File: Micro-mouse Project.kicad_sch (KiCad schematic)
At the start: 29 parts, among them IC1 CH224K, J1 Conn_02x16_Odd_Even, J3 USB_C_Receptacle_USB2.0_16P, Q2 2N3904, U2 LM2596S-5, U4 INA219AxD, U7 TP4056-42-ESOP8

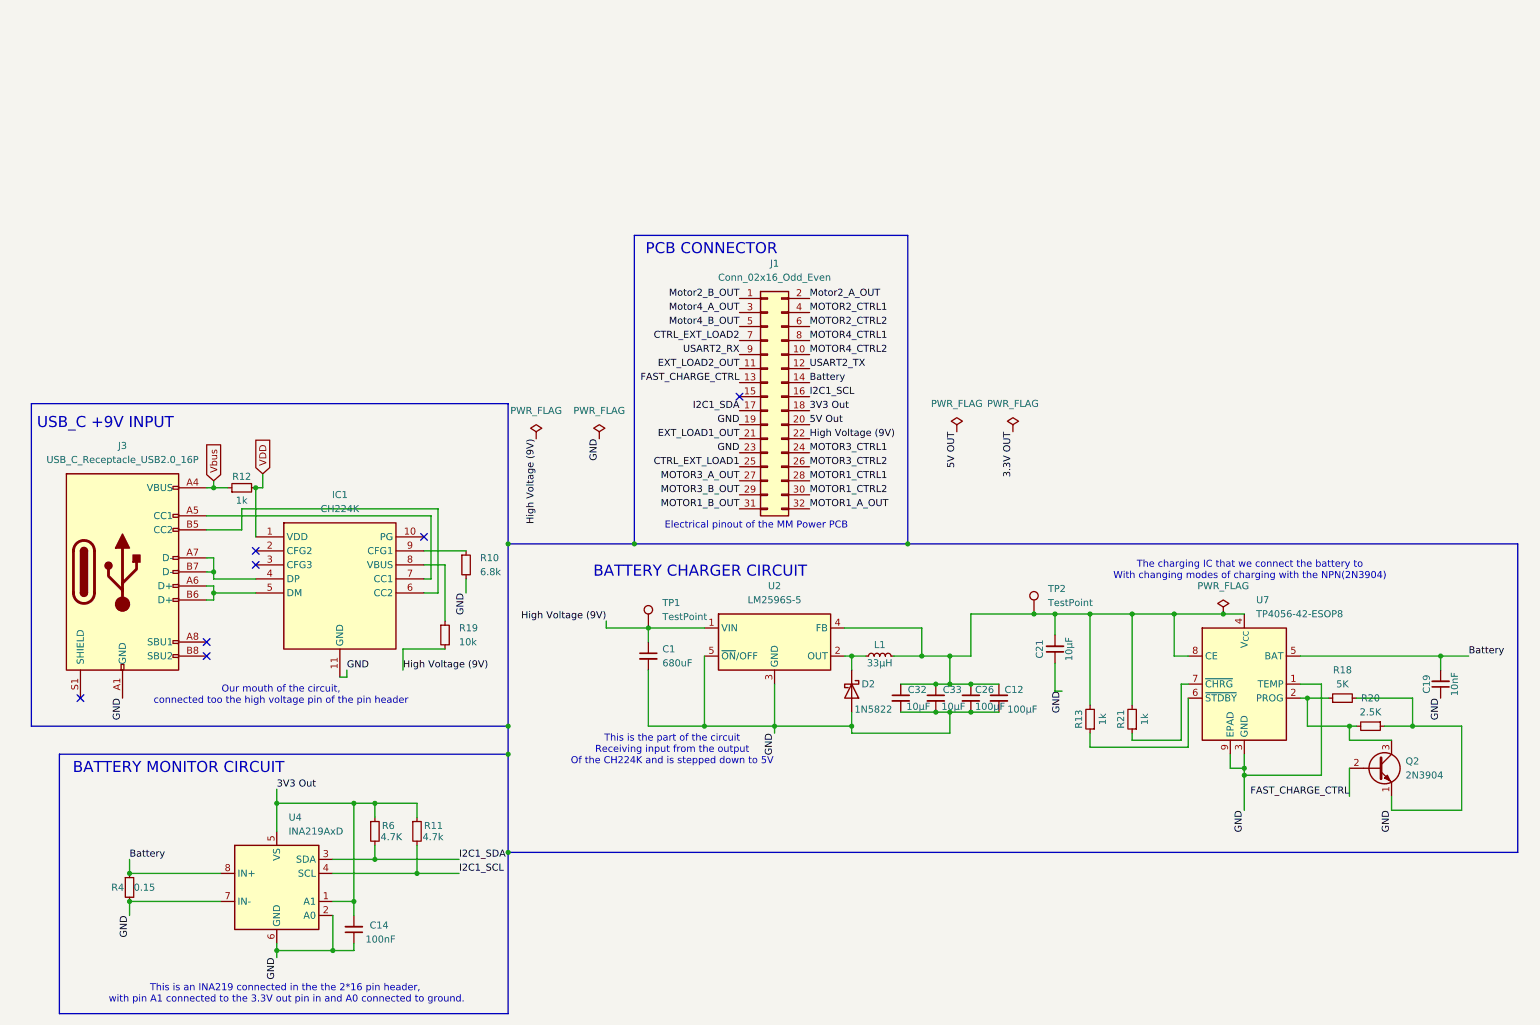
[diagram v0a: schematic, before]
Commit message: The Motor Management Circuit
This caters for the motor and the switching ON/OFF of the power subsystem.
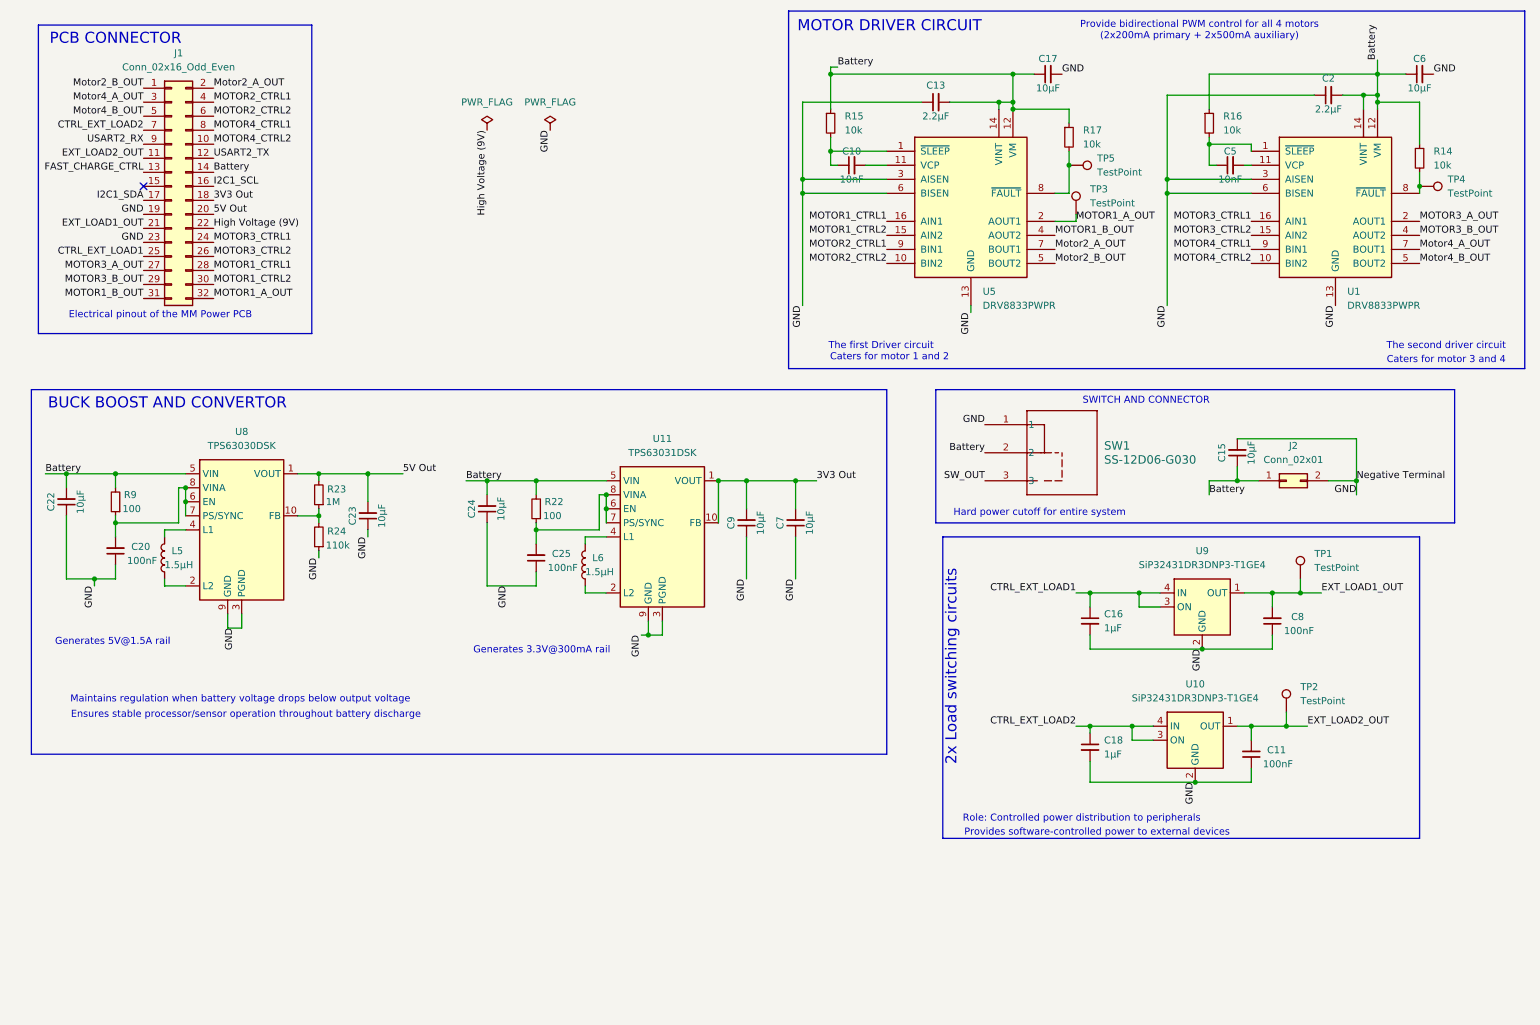
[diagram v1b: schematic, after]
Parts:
- removed C1: 680uF, Capacitor_THT:CP_Axial_L18.0mm_D10.0mm_P25.00mm_Horizontal, symbol Device:C_Small
- removed C12, C26: 100μF, Capacitor_SMD:C_1206_3216Metric_Pad1.33x1.80mm_HandSolder, symbol Device:C_Small
- removed C14: 100nF, Capacitor_SMD:C_0402_1005Metric_Pad0.74x0.62mm_HandSolder, symbol Device:C_Small
- removed C19: 10nF, Capacitor_SMD:C_0805_2012Metric_Pad1.18x1.45mm_HandSolder, symbol Device:C_Small
- removed C21: 10μF, Capacitor_SMD:C_1206_3216Metric_Pad1.33x1.80mm_HandSolder, symbol Device:C_Small
- removed C32, C33: 10μF, Capacitor_SMD:C_0805_2012Metric_Pad1.18x1.45mm_HandSolder, symbol Device:C_Small
- removed D2: 1N5822, Library:DIO_SS34, symbol Diode:1N5822
- removed IC1: CH224K, Library:SOP100P600X180-11N, symbol CH224K:CH224K
- removed J3: USB_C_Receptacle_USB2.0_16P, Connector_USB:USB_C_Receptacle_GCT_USB4105-xx-A_16P_TopMnt_Horizontal, symbol Connector:USB_C_Receptacle_USB2.0_16P
- removed L1: 33μH, Inductor_THT:L_Axial_L20.0mm_D8.0mm_P25.40mm_Horizontal, symbol Device:L_Small
- removed Q2: 2N3904, Package_TO_SOT_SMD:SOT-23, symbol Transistor_BJT:2N3904
- removed R10: 6.8k, Resistor_SMD:R_0603_1608Metric_Pad0.98x0.95mm_HandSolder, symbol Device:R_Small
- removed R11: 4.7k, Resistor_SMD:R_0603_1608Metric_Pad0.98x0.95mm_HandSolder, symbol Device:R_Small
- removed R12, R13, R21: 1k, Resistor_SMD:R_1206_3216Metric_Pad1.30x1.75mm_HandSolder, symbol Device:R_Small
- removed R18: 5K, Resistor_SMD:R_0603_1608Metric, symbol Device:R_Small
- removed R19: 10k, Resistor_SMD:R_0805_2012Metric_Pad1.20x1.40mm_HandSolder, symbol Device:R_Small
- removed R20: 2.5K, Resistor_SMD:R_0603_1608Metric, symbol Device:R_Small
- removed R4: 0.15, Resistor_SMD:R_1206_3216Metric_Pad1.30x1.75mm_HandSolder, symbol Device:R_Small
- removed R6: 4.7K, Resistor_SMD:R_0603_1608Metric_Pad0.98x0.95mm_HandSolder, symbol Device:R_Small
- removed U2: LM2596S-5, Package_TO_SOT_SMD:TO-263-5_TabPin3, symbol Regulator_Switching:LM2596S-5
- removed U4: INA219AxD, Library:SOT65P280X145-8N, symbol Sensor_Energy:INA219AxD
- removed U7: TP4056-42-ESOP8, Library:SOIC127P600X175-9N, symbol Battery_Management:TP4056-42-ESOP8
- added C10, C5: 10nF, Capacitor_SMD:C_0805_2012Metric_Pad1.18x1.45mm_HandSolder, symbol Device:C_Small
- added C11, C20, C25, C8: 100nF, Capacitor_SMD:C_0402_1005Metric_Pad0.74x0.62mm_HandSolder, symbol Device:C_Small
- added C13, C2: 2.2μF, Capacitor_SMD:C_0402_1005Metric_Pad0.74x0.62mm_HandSolder, symbol Device:C_Small
- added C15, C17, C22, C23, C24, C6, C7, C9: 10μF, Capacitor_SMD:C_1206_3216Metric_Pad1.33x1.80mm_HandSolder, symbol Device:C_Small
- added C16, C18: 1μF, Capacitor_SMD:C_1206_3216Metric_Pad1.33x1.80mm_HandSolder, symbol Device:C_Small
- added J2: Conn_02x01, symbol Connector_Generic:Conn_02x01
- added L5, L6: 1.5µH, Inductor_SMD:L_1206_3216Metric_Pad1.22x1.90mm_HandSolder, symbol Device:L
- added R14, R15, R16, R17: 10k, Resistor_SMD:R_0805_2012Metric_Pad1.20x1.40mm_HandSolder, symbol Device:R_Small
- added R22, R9: 100, Resistor_SMD:R_0805_2012Metric_Pad1.20x1.40mm_HandSolder, symbol Device:R_Small
- added R23: 1M, Resistor_SMD:R_1206_3216Metric_Pad1.30x1.75mm_HandSolder, symbol Device:R_Small
- added R24: 110k, Resistor_SMD:R_0805_2012Metric_Pad1.20x1.40mm_HandSolder, symbol Device:R_Small
- added SW1: SS-12D06-G030, Library:SS-12D06_GSW, symbol 2025-03-28_06-57-30:SS-12D06-G030
- added TP3, TP4, TP5: TestPoint, symbol Connector:TestPoint
- added U1, U5: DRV8833PWPR, Library:IC_DRV8833PWPR, symbol Driver_Motor:DRV8833PWP
- added U10: SiP32431DR3DNP3-T1GE4, Library:SON50P120X160X60-5N, symbol Power_Management:SiP32431DR3
- added U11: TPS63031DSK, Package_SON:WSON-10-1EP_2.5x2.5mm_P0.5mm_EP1.2x2mm, symbol Regulator_Switching:TPS63031DSK
- added U8: TPS63030DSK, Package_SON:WSON-10-1EP_2.5x2.5mm_P0.5mm_EP1.2x2mm, symbol Regulator_Switching:TPS63030DSK
- added U9: SiP32431DR3DNP3-T1GE4, Package_TO_SOT_SMD:SOT-363_SC-70-6, symbol Power_Management:SiP32431DR3
- J1: footprint Connector_PinHeader_2.54mm:PinHeader_2x16_P2.54mm_Vertical -> (none)
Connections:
- net 3V3 Out: now also C7.2, C9.2, U11.1 (VOUT), U11.10 (FB)
- net 5V Out: now also C23.2, R23.2, U8.1 (VOUT)
- net Battery: now also C13.2, C15.1, C17.1, C2.2, C22.2, C24.2, C6.1, J2.1 (Pin_1), R14.1, R15.1, R16.1, R17.1, R22.2, R9.2, SW1.2, U1.12 (VM), U1.14 (VINT), U11.5 (VIN), U5.12 (VM), U5.14 (VINT), U8.5 (VIN)
- net CTRL_EXT_LOAD1: now also C16.1, U9.3 (ON), U9.4 (IN)
- net CTRL_EXT_LOAD2: now also C18.1, U10.3 (ON), U10.4 (IN)
- net EXT_LOAD1_OUT: now also TP1.1, C8.2, U9.1 (OUT)
- net EXT_LOAD2_OUT: now also TP2.1, C11.2, U10.1 (OUT)
- net GND: now also C11.1, C13.1, C15.2, C16.2, C17.2, C18.2, C2.1, C20.1, C22.1, C23.1, C24.1, C25.1, C6.2, C7.1, C8.1, C9.1, J2.2 (Pin_2), R24.1, SW1.1, U1.13 (GND), U1.17 (GND), U1.3 (AISEN), U1.6 (BISEN), U10.2 (GND), U10.5 (GND), U11.11 (PGND), U11.3 (PGND), U11.9 (GND), U5.13 (GND), U5.17 (GND), U5.3 (AISEN), U5.6 (BISEN), U8.11 (PGND), U8.3 (PGND), U8.9 (GND), U9.2 (GND), U9.5 (GND)
- net High Voltage (9V): no longer TP1.1
- net MOTOR1_A_OUT: now also TP3.1, U5.2 (AOUT1)
- net MOTOR1_B_OUT: now also U5.4 (AOUT2)
- net MOTOR1_CTRL1: now also U5.16 (AIN1)
- net MOTOR1_CTRL2: now also U5.15 (AIN2)
- net MOTOR2_CTRL1: now also U5.9 (BIN1)
- net MOTOR2_CTRL2: now also U5.10 (BIN2)
- net MOTOR3_A_OUT: now also U1.2 (AOUT1)
- net MOTOR3_B_OUT: now also U1.4 (AOUT2)
- net MOTOR3_CTRL1: now also U1.16 (AIN1)
- net MOTOR3_CTRL2: now also U1.15 (AIN2)
- net MOTOR4_CTRL1: now also U1.9 (BIN1)
- net MOTOR4_CTRL2: now also U1.10 (BIN2)
- net Motor2_A_OUT: now also U5.7 (BOUT1)
- net Motor2_B_OUT: now also U5.5 (BOUT2)
- net Motor4_A_OUT: now also U1.7 (BOUT1)
- net Motor4_B_OUT: now also U1.5 (BOUT2)
- new net: R17.2, TP5.1, U5.8 (~{FAULT})
- new net: C20.2, R9.1, U8.6 (EN), U8.7 (PS/SYNC), U8.8 (VINA)
- new net: C10.1, R15.2, U5.1 (~{SLEEP})
- new net: R23.1, R24.2, U8.10 (FB)
- new net: L6.1, U11.2 (L2)
- new net: L6.2, U11.4 (L1)
- new net: C5.1, R16.2, U1.1 (~{SLEEP})
- new net: C5.2, U1.11 (VCP)
- new net: R14.2, TP4.1, U1.8 (~{FAULT})
- new net: L5.1, U8.2 (L2)
- new net: L5.2, U8.4 (L1)
- new net: C10.2, U5.11 (VCP)
- new net: C25.2, R22.1, U11.6 (EN), U11.7 (PS/SYNC), U11.8 (VINA)
- new net SW_OUT: SW1.3
- no-connect marks 7 -> 1
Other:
- note added: "2x Load switching circuits"
- note added: "BUCK BOOST AND CONVERTOR"
- note added: "Caters for motor 1 and 2"
- note added: "Caters for motor 3 and 4"
- note added: "Ensures stable processor/sensor operation throughout battery discharge"
- note added: "Generates 3.3V@300mA rail"
- note added: "Generates 5V@1.5A rail"
- note added: "Hard power cutoff for entire system"
- note added: "MOTOR DRIVER CIRCUIT"
- note added: "Maintains regulation when battery voltage drops below output voltage"
- note added: "Provide bidirectional PWM control for all 4 motors (2x200mA primary + 2x500mA auxiliary)"
- note added: "Provides software-controlled power to external devices"
- note added: "Role: Controlled power distribution to peripherals"
- note added: "SWITCH AND CONNECTOR"
- note added: "The first Driver circuit"
- note added: "The second driver circuit"
- note removed: "BATTERY CHARGER CIRCUIT"
- note removed: "BATTERY MONITOR CIRCUIT"
- note removed: "Our mouth of the circuit, connected too the high voltage pin of the pin header"
- note removed: "The charging IC that we connect the battery to With changing modes of charging with the NPN(2N3904)"
- note removed: "This is an INA219 connected in the the 2*16 pin header, with pin A1 connected to the 3.3V out pin in and A0 connected to ground."
- note removed: "This is the part of the circuit Receiving input from the output Of the CH224K and is stepped down to 5V"
- note removed: "USB_C +9V INPUT"
- moved on the sheet: J1
